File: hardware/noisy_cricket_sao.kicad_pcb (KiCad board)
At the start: 2 copper layers, 30 x 25 mm, 23 parts, among them J1 SAO 6-Pin, U1 AD8107, U3 MSPM0C1104SDYYR

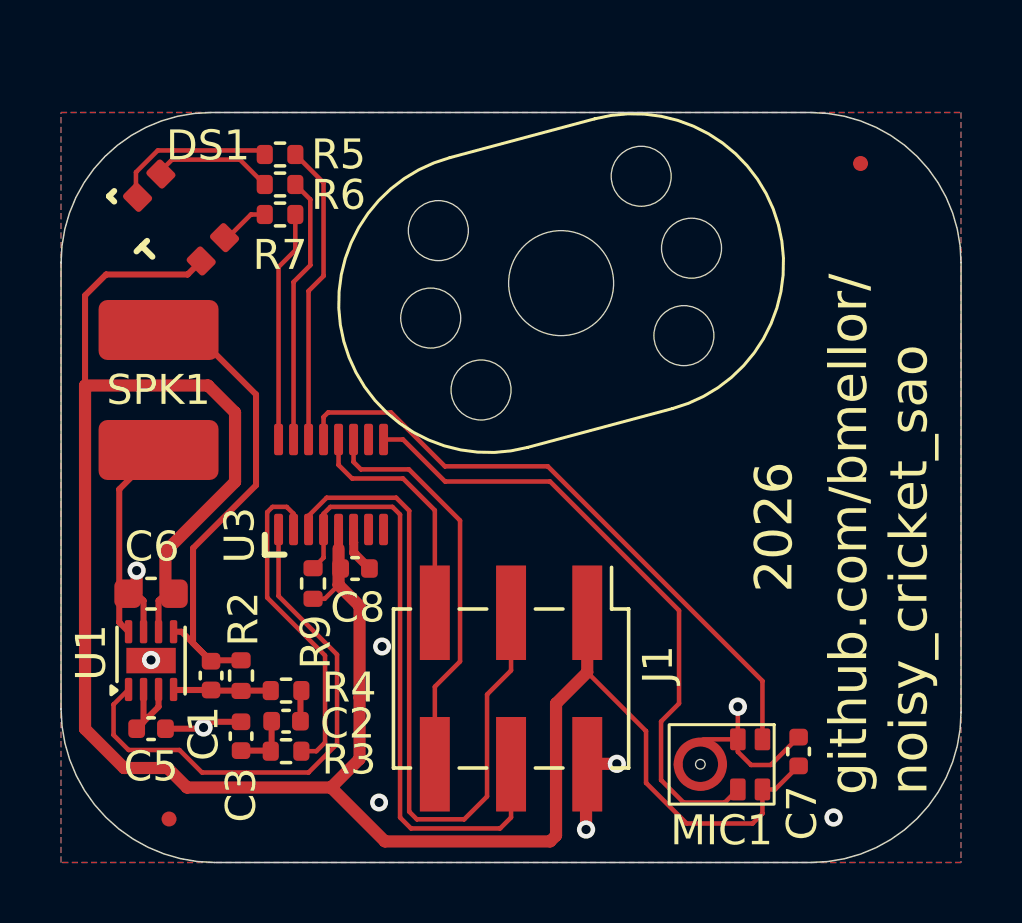
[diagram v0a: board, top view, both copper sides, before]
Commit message: fix short in layout
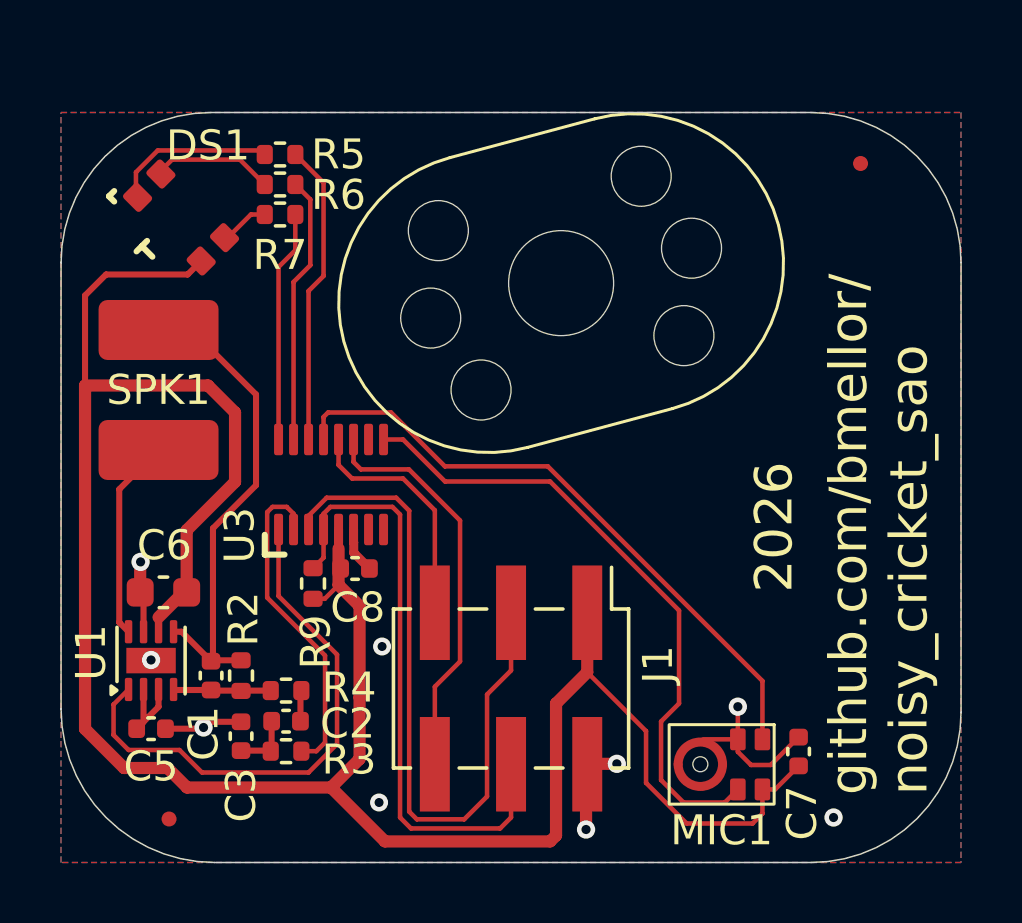
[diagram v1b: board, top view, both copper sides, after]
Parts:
- moved C6 0.42 mm to (129.4, 95.0)
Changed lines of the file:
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@@
 	(footprint "Capacitor_SMD:C_0603_1608Metric"
 		(layer "F.Cu")
-		(at 129 95.04 180)
+		(at 129.413 94.996 180)
 		(descr "Capacitor SMD 0603 (1608 Metric), square (rectangular) end terminal, IPC-7351 nominal, (Body size source: IPC-SM-782 page 76, https://www.pcb-3d.com/wordpress/wp-content/uploads/ipc-sm-782a_amendment_1_and_2.pdf)")
 		(tags "capacitor")
@@
 		(pad "" np_thru_hole circle
 			(at -0.005 0.71 270)
-			(size 0.32 0.32)
-			(drill 0.32)
+			(size 0.5 0.5)
+			(drill 0.5)
 			(layers "*.Cu" "*.Mask")
 			(solder_mask_margin 0.15)
@@
 	)
 	(segment
+		(start 131.8 91.3125)
+		(end 131.8 89)
+		(width 0.4064)
+		(layer "F.Cu")
+		(net "+3V3")
+	)
+	(segment
 		(start 126.8 85.1)
 		(end 126.8 88.1)
@@
 	)
 	(segment
-		(start 131.8 91.3125)
-		(end 131.8 89)
-		(width 0.4064)
+		(start 149.05 102.7)
+		(end 146.854342 102.7)
+		(width 0.1524)
 		(layer "F.Cu")
 		(net "+3V3")
 	)
 	(segment
-		(start 129.48 93.6325)
-		(end 131.8 91.3125)
+		(start 130.188 94.888986)
+		(end 130.188 92.9245)
 		(width 0.4064)
 		(layer "F.Cu")
@@
 	)
 	(segment
-		(start 149.05 102.7)
-		(end 146.854342 102.7)
-		(width 0.1524)
+		(start 143.54 96.175)
+		(end 143.54 97.66)
+		(width 0.4064)
 		(layer "F.Cu")
 		(net "+3V3")
 	)
 	(segment
-		(start 143.54 96.175)
-		(end 143.54 97.66)
+		(start 129.25 95.826986)
+		(end 130.188 94.888986)
 		(width 0.4064)
 		(layer "F.Cu")
@@
 	)
 	(segment
-		(start 131.8 89)
-		(end 130.9 88.1)
-		(width 0.4064)
-		(layer "F.Cu")
-		(net "+3V3")
-	)
-	(segment
 		(start 145.5 99.62)
 		(end 143.54 97.66)
@@
 	)
 	(segment
-		(start 129.25 96.3075)
-		(end 129.25 95.27)
-		(width 0.2032)
-		(layer "F.Cu")
-		(net "+3V3")
-	)
-	(segment
 		(start 128.1 100.85)
 		(end 129.55 100.85)
@@
 	)
 	(segment
-		(start 129.48 95.04)
-		(end 129.48 93.6325)
-		(width 0.4064)
-		(layer "F.Cu")
-		(net "+3V3")
-	)
-	(segment
 		(start 127.5 84.4)
 		(end 126.8 85.1)
@@
 	)
 	(segment
-		(start 129.25 95.27)
-		(end 129.48 95.04)
-		(width 0.2032)
+		(start 135.95 95.45)
+		(end 135.25 94.75)
+		(width 0.4064)
 		(layer "F.Cu")
 		(net "+3V3")
 	)
 	(segment
-		(start 135.95 95.45)
-		(end 135.25 94.75)
+		(start 130.188 92.9245)
+		(end 131.8 91.3125)
 		(width 0.4064)
 		(layer "F.Cu")
@@
 	)
 	(segment
+		(start 131.8 89)
+		(end 130.9 88.1)
+		(width 0.4064)
+		(layer "F.Cu")
+		(net "+3V3")
+	)
+	(segment
 		(start 142.5 103.1)
 		(end 142.3032 103.2968)
@@
 	)
 	(segment
+		(start 129.25 96.3075)
+		(end 129.25 95.826986)
+		(width 0.2032)
+		(layer "F.Cu")
+		(net "+3V3")
+	)
+	(segment
 		(start 149.379999 101.565)
 		(end 149.799895 101.565)
@@
 	)
 	(segment
+		(start 128.638 93.993)
+		(end 128.651 93.98)
+		(width 0.4064)
+		(layer "F.Cu")
+		(net "GND")
+	)
+	(segment
+		(start 128.638 94.922)
+		(end 128.638 93.993)
+		(width 0.4064)
+		(layer "F.Cu")
+		(net "GND")
+	)
+	(segment
 		(start 144.526 100.711)
 		(end 143.554 100.711)
@@
 	)
 	(segment
-		(start 128.52 95.04)
-		(end 128.52 94.27)
-		(width 0.4064)
-		(layer "F.Cu")
-		(net "GND")
-	)
-	(segment
 		(start 130.71 99.54)
 		(end 130.75 99.5)
@@
 	)
 	(segment
+		(start 128.52 95.04)
+		(end 128.638 94.922)
+		(width 0.4064)
+		(layer "F.Cu")
+		(net "GND")
+	)
+	(segment
 		(start 149.654895 100.75)
 		(end 150.584895 99.82)
@@
 	)
 	(via
-		(at 128.52 94.27)
+		(at 128.651 93.98)
 		(size 0.6096)
 		(drill 0.3048)
@@
 	)
 	(segment
-		(start 129.75 96.3075)
-		(end 130.0175 96.3075)
+		(start 131.064 97.166)
+		(end 130.97 97.26)
 		(width 0.2032)
 		(layer "F.Cu")
@@
 	)
 	(segment
-		(start 130.35 86.25)
-		(end 132.5 88.4)
+		(start 129.75 96.3075)
+		(end 130.0175 96.3075)
 		(width 0.2032)
 		(layer "F.Cu")
@@
 	)
 	(segment
-		(start 129.25 86.25)
-		(end 130.35 86.25)
+		(start 130.97 97.26)
+		(end 132 97.26)
 		(width 0.2032)
 		(layer "F.Cu")
@@
 	)
 	(segment
-		(start 130.4 93.525)
-		(end 130.4 96.69)
+		(start 130.0175 96.3075)
+		(end 131 97.29)
 		(width 0.2032)
 		(layer "F.Cu")
@@
 	)
 	(segment
-		(start 130.97 97.26)
-		(end 132 97.26)
+		(start 132.5 88.4)
+		(end 132.5 91.425)
 		(width 0.2032)
 		(layer "F.Cu")
@@
 	)
 	(segment
-		(start 130.0175 96.3075)
-		(end 131 97.29)
+		(start 132.5 91.425)
+		(end 131.064 92.861)
 		(width 0.2032)
 		(layer "F.Cu")
@@
 	)
 	(segment
-		(start 132.5 91.425)
-		(end 130.4 93.525)
+		(start 129.25 86.25)
+		(end 130.35 86.25)
 		(width 0.2032)
 		(layer "F.Cu")
@@
 	)
 	(segment
-		(start 130.4 96.69)
-		(end 130.97 97.26)
+		(start 131.064 92.861)
+		(end 131.064 97.166)
 		(width 0.2032)
 		(layer "F.Cu")
@@
 	)
 	(segment
-		(start 132.5 88.4)
-		(end 132.5 91.425)
+		(start 130.35 86.25)
+		(end 132.5 88.4)
 		(width 0.2032)
 		(layer "F.Cu")
